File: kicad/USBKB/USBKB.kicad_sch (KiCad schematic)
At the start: 70 parts, among them K0 KAILH_CPG151101S11, K1 KAILH_CPG151101S11, K2 KAILH_CPG151101S11, K3 KAILH_CPG151101S11, K4 KAILH_CPG151101S11, K5 KAILH_CPG151101S11, K6 KAILH_CPG151101S11, K7 KAILH_CPG151101S11, K8 KAILH_CPG151101S11, K9 KAILH_CPG151101S11, U1 ATMEGA32U4-MU, U2 ICSP, U70 UJ31-CH-G2-SMT-TR, Y1 Crystal_GND23

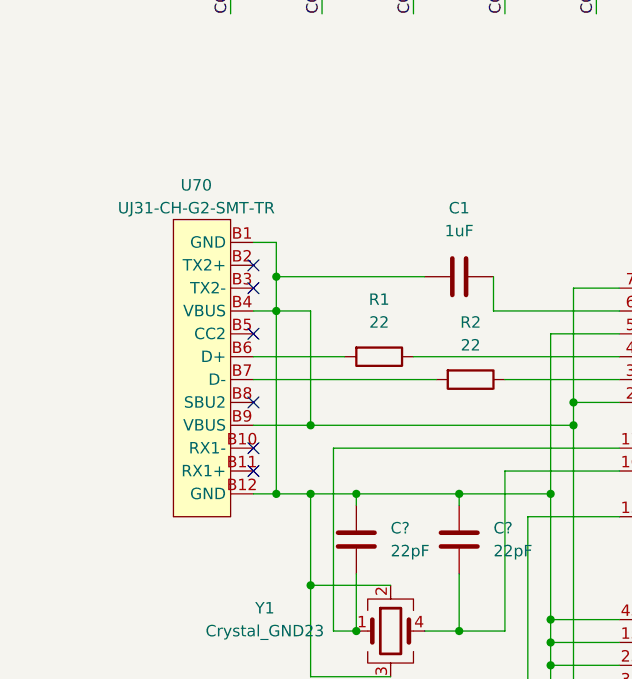
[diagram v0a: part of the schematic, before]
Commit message: Fixed USB-C connector in schematic
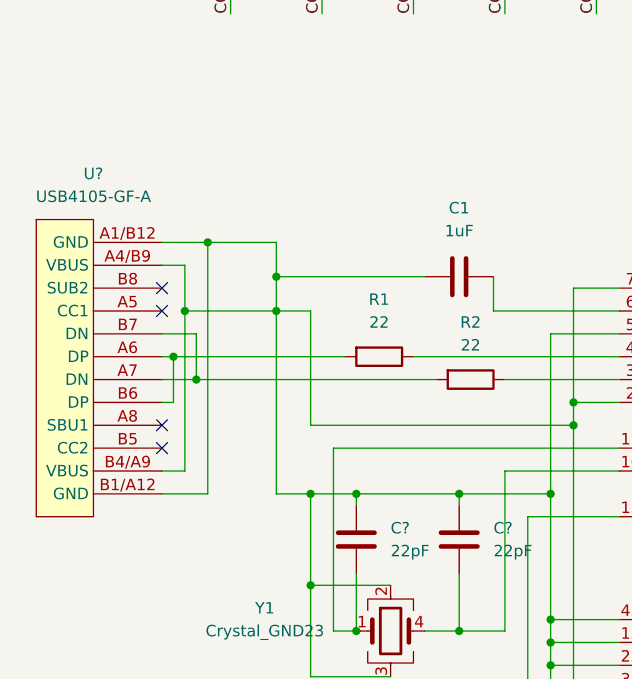
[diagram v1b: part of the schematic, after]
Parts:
- U?: renamed from U70; value UJ31-CH-G2-SMT-TR -> USB4105-GF-A; symbol USBKB:UJ31-CH-G2-SMT-TR -> USBKB:USB4105-GF-A
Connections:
- net at C1.1, C?.1, C?.1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: now also U?.A1/B12 (GND), U?.A4/B9 (VBUS), U?.B1/A12 (GND), U?.B4/A9 (VBUS); no longer U?.B1 (GND), U?.B12 (GND), U?.B4 (VBUS), U?.B9 (VBUS)
- net at R2.2, U?.B7 (DN): now also U?.A7 (DN)
- net at R1.2, U?.B6 (DP): now also U?.A6 (DP)
- no-connect marks 13 -> 11
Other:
- moved on the sheet: U?
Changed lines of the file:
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@@
   (junction (at 76.2 41.91) (diameter 0) (color 0 0 0 0)
   )
+  (junction (at 31.75 109.22) (diameter 0) (color 0 0 0 0)
+  )
   (junction (at 119.38 52.07) (diameter 0) (color 0 0 0 0)
   )
@@
   (junction (at 78.74 60.96) (diameter 0) (color 0 0 0 0)
   )
+  (junction (at 33.02 93.98) (diameter 0) (color 0 0 0 0)
+  )
   (junction (at 55.88 33.02) (diameter 0) (color 0 0 0 0)
   )
@@
   (junction (at 137.16 41.91) (diameter 0) (color 0 0 0 0)
   )
+  (junction (at 30.48 101.6) (diameter 0) (color 0 0 0 0)
+  )
   (junction (at 129.54 25.4) (diameter 0) (color 0 0 0 0)
   )
@@
   (junction (at 27.94 43.18) (diameter 0) (color 0 0 0 0)
   )
-  (junction (at 44.45 114.3) (diameter 0) (color 0 0 0 0)
-  )
   (junction (at 116.84 33.02) (diameter 0) (color 0 0 0 0)
   )
@@
   (junction (at 44.45 132.08) (diameter 0) (color 0 0 0 0)
   )
+  (junction (at 29.21 106.68) (diameter 0) (color 0 0 0 0)
+  )
   (junction (at 38.1 60.96) (diameter 0) (color 0 0 0 0)
   )
@@
   (junction (at 68.58 25.4) (diameter 0) (color 0 0 0 0)
   )
-  (junction (at 40.64 121.92) (diameter 0) (color 0 0 0 0)
-  )
   (junction (at 58.42 34.29) (diameter 0) (color 0 0 0 0)
   )
@@
   (junction (at 66.04 33.02) (diameter 0) (color 0 0 0 0)
   )
-  (no_connect (at 38.1 104.14))
-  (no_connect (at 38.1 99.06))
-  (no_connect (at 38.1 116.84))
-  (no_connect (at 38.1 119.38))
-  (no_connect (at 38.1 96.52))
-  (no_connect (at 38.1 111.76))
+  (no_connect (at 27.94 114.3))
+  (no_connect (at 27.94 116.84))
+  (no_connect (at 27.94 101.6))
+  (no_connect (at 27.94 99.06))
   (no_connect (at 121.92 95.25))
   (no_connect (at 121.92 146.05))
@@
     (stroke (width 0) (type default) (color 0 0 0 0))
   )
-  (wire (pts (xy 38.1 121.92) (xy 40.64 121.92))
-    (stroke (width 0) (type default) (color 0 0 0 0))
-  )
   (wire (pts (xy 149.86 24.13) (xy 149.86 25.4))
     (stroke (width 0) (type default) (color 0 0 0 0))
   )
+  (wire (pts (xy 33.02 121.92) (xy 33.02 93.98))
+    (stroke (width 0) (type default) (color 0 0 0 0))
+  )
   (wire (pts (xy 40.64 101.6) (xy 40.64 121.92))
     (stroke (width 0) (type default) (color 0 0 0 0))
@@
     (stroke (width 0) (type default) (color 0 0 0 0))
   )
+  (wire (pts (xy 29.21 111.76) (xy 29.21 106.68))
+    (stroke (width 0) (type default) (color 0 0 0 0))
+  )
   (wire (pts (xy 68.58 34.29) (xy 68.58 33.02))
     (stroke (width 0) (type default) (color 0 0 0 0))
@@
     (stroke (width 0) (type default) (color 0 0 0 0))
   )
-  (wire (pts (xy 38.1 106.68) (xy 48.26 106.68))
+  (wire (pts (xy 29.21 106.68) (xy 48.26 106.68))
     (stroke (width 0) (type default) (color 0 0 0 0))
   )
@@
     (stroke (width 0) (type default) (color 0 0 0 0))
   )
+  (wire (pts (xy 31.75 104.14) (xy 27.94 104.14))
+    (stroke (width 0) (type default) (color 0 0 0 0))
+  )
   (wire (pts (xy 48.26 52.07) (xy 58.42 52.07))
     (stroke (width 0) (type default) (color 0 0 0 0))
@@
     (stroke (width 0) (type default) (color 0 0 0 0))
   )
-  (wire (pts (xy 38.1 101.6) (xy 40.64 101.6))
+  (wire (pts (xy 30.48 101.6) (xy 40.64 101.6))
     (stroke (width 0) (type default) (color 0 0 0 0))
   )
@@
     (stroke (width 0) (type default) (color 0 0 0 0))
   )
+  (wire (pts (xy 27.94 109.22) (xy 31.75 109.22))
+    (stroke (width 0) (type default) (color 0 0 0 0))
+  )
   (wire (pts (xy 121.92 161.29) (xy 128.27 161.29))
     (stroke (width 0) (type default) (color 0 0 0 0))
@@
     (stroke (width 0) (type default) (color 0 0 0 0))
   )
-  (wire (pts (xy 38.1 114.3) (xy 44.45 114.3))
-    (stroke (width 0) (type default) (color 0 0 0 0))
-  )
   (wire (pts (xy 27.94 34.29) (xy 38.1 34.29))
     (stroke (width 0) (type default) (color 0 0 0 0))
@@
     (stroke (width 0) (type default) (color 0 0 0 0))
   )
+  (wire (pts (xy 27.94 96.52) (xy 30.48 96.52))
+    (stroke (width 0) (type default) (color 0 0 0 0))
+  )
   (wire (pts (xy 109.22 52.07) (xy 109.22 50.8))
     (stroke (width 0) (type default) (color 0 0 0 0))
@@
     (stroke (width 0) (type default) (color 0 0 0 0))
   )
+  (wire (pts (xy 31.75 109.22) (xy 31.75 104.14))
+    (stroke (width 0) (type default) (color 0 0 0 0))
+  )
   (wire (pts (xy 121.92 118.11) (xy 132.08 118.11))
     (stroke (width 0) (type default) (color 0 0 0 0))
@@
     (stroke (width 0) (type default) (color 0 0 0 0))
   )
-  (wire (pts (xy 40.64 93.98) (xy 38.1 93.98))
+  (wire (pts (xy 33.02 93.98) (xy 27.94 93.98))
+    (stroke (width 0) (type default) (color 0 0 0 0))
+  )
+  (wire (pts (xy 33.02 93.98) (xy 40.64 93.98))
     (stroke (width 0) (type default) (color 0 0 0 0))
   )
@@
     (stroke (width 0) (type default) (color 0 0 0 0))
   )
-  (wire (pts (xy 38.1 109.22) (xy 58.42 109.22))
+  (wire (pts (xy 31.75 109.22) (xy 58.42 109.22))
     (stroke (width 0) (type default) (color 0 0 0 0))
   )
@@
     (stroke (width 0) (type default) (color 0 0 0 0))
   )
+  (wire (pts (xy 30.48 119.38) (xy 27.94 119.38))
+    (stroke (width 0) (type default) (color 0 0 0 0))
+  )
   (wire (pts (xy 48.26 34.29) (xy 48.26 33.02))
     (stroke (width 0) (type default) (color 0 0 0 0))
@@
     (stroke (width 0) (type default) (color 0 0 0 0))
   )
+  (wire (pts (xy 27.94 121.92) (xy 33.02 121.92))
+    (stroke (width 0) (type default) (color 0 0 0 0))
+  )
   (wire (pts (xy 121.92 115.57) (xy 134.62 115.57))
     (stroke (width 0) (type default) (color 0 0 0 0))
@@
     (stroke (width 0) (type default) (color 0 0 0 0))
   )
+  (wire (pts (xy 30.48 96.52) (xy 30.48 101.6))
+    (stroke (width 0) (type default) (color 0 0 0 0))
+  )
   (wire (pts (xy 78.74 143.51) (xy 71.12 143.51))
     (stroke (width 0) (type default) (color 0 0 0 0))
   )
+  (wire (pts (xy 29.21 106.68) (xy 27.94 106.68))
+    (stroke (width 0) (type default) (color 0 0 0 0))
+  )
   (wire (pts (xy 129.54 43.18) (xy 139.7 43.18))
     (stroke (width 0) (type default) (color 0 0 0 0))
@@
     (stroke (width 0) (type default) (color 0 0 0 0))
   )
+  (wire (pts (xy 27.94 111.76) (xy 29.21 111.76))
+    (stroke (width 0) (type default) (color 0 0 0 0))
+  )
   (wire (pts (xy 129.54 60.96) (xy 139.7 60.96))
     (stroke (width 0) (type default) (color 0 0 0 0))
@@
   )
   (wire (pts (xy 55.88 106.68) (xy 78.74 106.68))
+    (stroke (width 0) (type default) (color 0 0 0 0))
+  )
+  (wire (pts (xy 30.48 101.6) (xy 30.48 119.38))
     (stroke (width 0) (type default) (color 0 0 0 0))
   )
@@
     (pin "2")
   )
-  (symbol (lib_id "USBKB:UJ31-CH-G2-SMT-TR") (at 35.56 107.95 0) (unit 1)
-    (in_bom yes) (on_board yes) (fields_autoplaced)
-    (property "Reference" "U70" (id 0) (at 31.75 87.63 0))
-    (property "Value" "UJ31-CH-G2-SMT-TR" (id 1) (at 31.75 90.17 0))
-    (property "Footprint" "USBKB:USB4105-GF-A" (id 2) (at 35.56 88.9 0)
-      (effects (font (size 1.27 1.27)) hide)
-    )
-    (property "Datasheet" "" (id 3) (at 35.56 88.9 0)
-      (effects (font (size 1.27 1.27)) hide)
-    )
-    (pin "B1")
-    (pin "B10")
-    (pin "B11")
-    (pin "B12")
-    (pin "B2")
-    (pin "B3")
-    (pin "B4")
+  (symbol (lib_id "USBKB:USB4105-GF-A") (at 20.32 99.06 0) (unit 1)
+    (in_bom yes) (on_board yes)
+    (property "Reference" "U?" (id 0) (at 20.32 86.36 0))
+    (property "Value" "USB4105-GF-A" (id 1) (at 20.32 88.9 0))
+    (property "Footprint" "USBKB:USB4105-GF-A" (id 2) (at 20.32 86.36 0)
+      (effects (font (size 1.27 1.27)) hide)
+    )
+    (property "Datasheet" "" (id 3) (at 20.32 86.36 0)
+      (effects (font (size 1.27 1.27)) hide)
+    )
+    (pin "A1/B12")
+    (pin "A4/B9")
+    (pin "A5")
+    (pin "A6")
+    (pin "A7")
+    (pin "A8")
+    (pin "B1/A12")
+    (pin "B4/A9")
     (pin "B5")
     (pin "B6")
     (pin "B7")
     (pin "B8")
-    (pin "B9")
   )
   (symbol (lib_id "USBKB:KAILH_CPG151101S11") (at 92.71 33.02 0) (unit 1)
@@
     )
     (path "/f359e712-bc14-4294-ae7c-f8c3b49e712a"
-      (reference "U70") (unit 1) (value "UJ31-CH-G2-SMT-TR") (footprint "USBKB:USB4105-GF-A")
+      (reference "U?") (unit 1) (value "USB4105-GF-A") (footprint "USBKB:USB4105-GF-A")
     )
     (path "/f8aa7b9d-0275-447c-a33e-2d8cb13a8083"

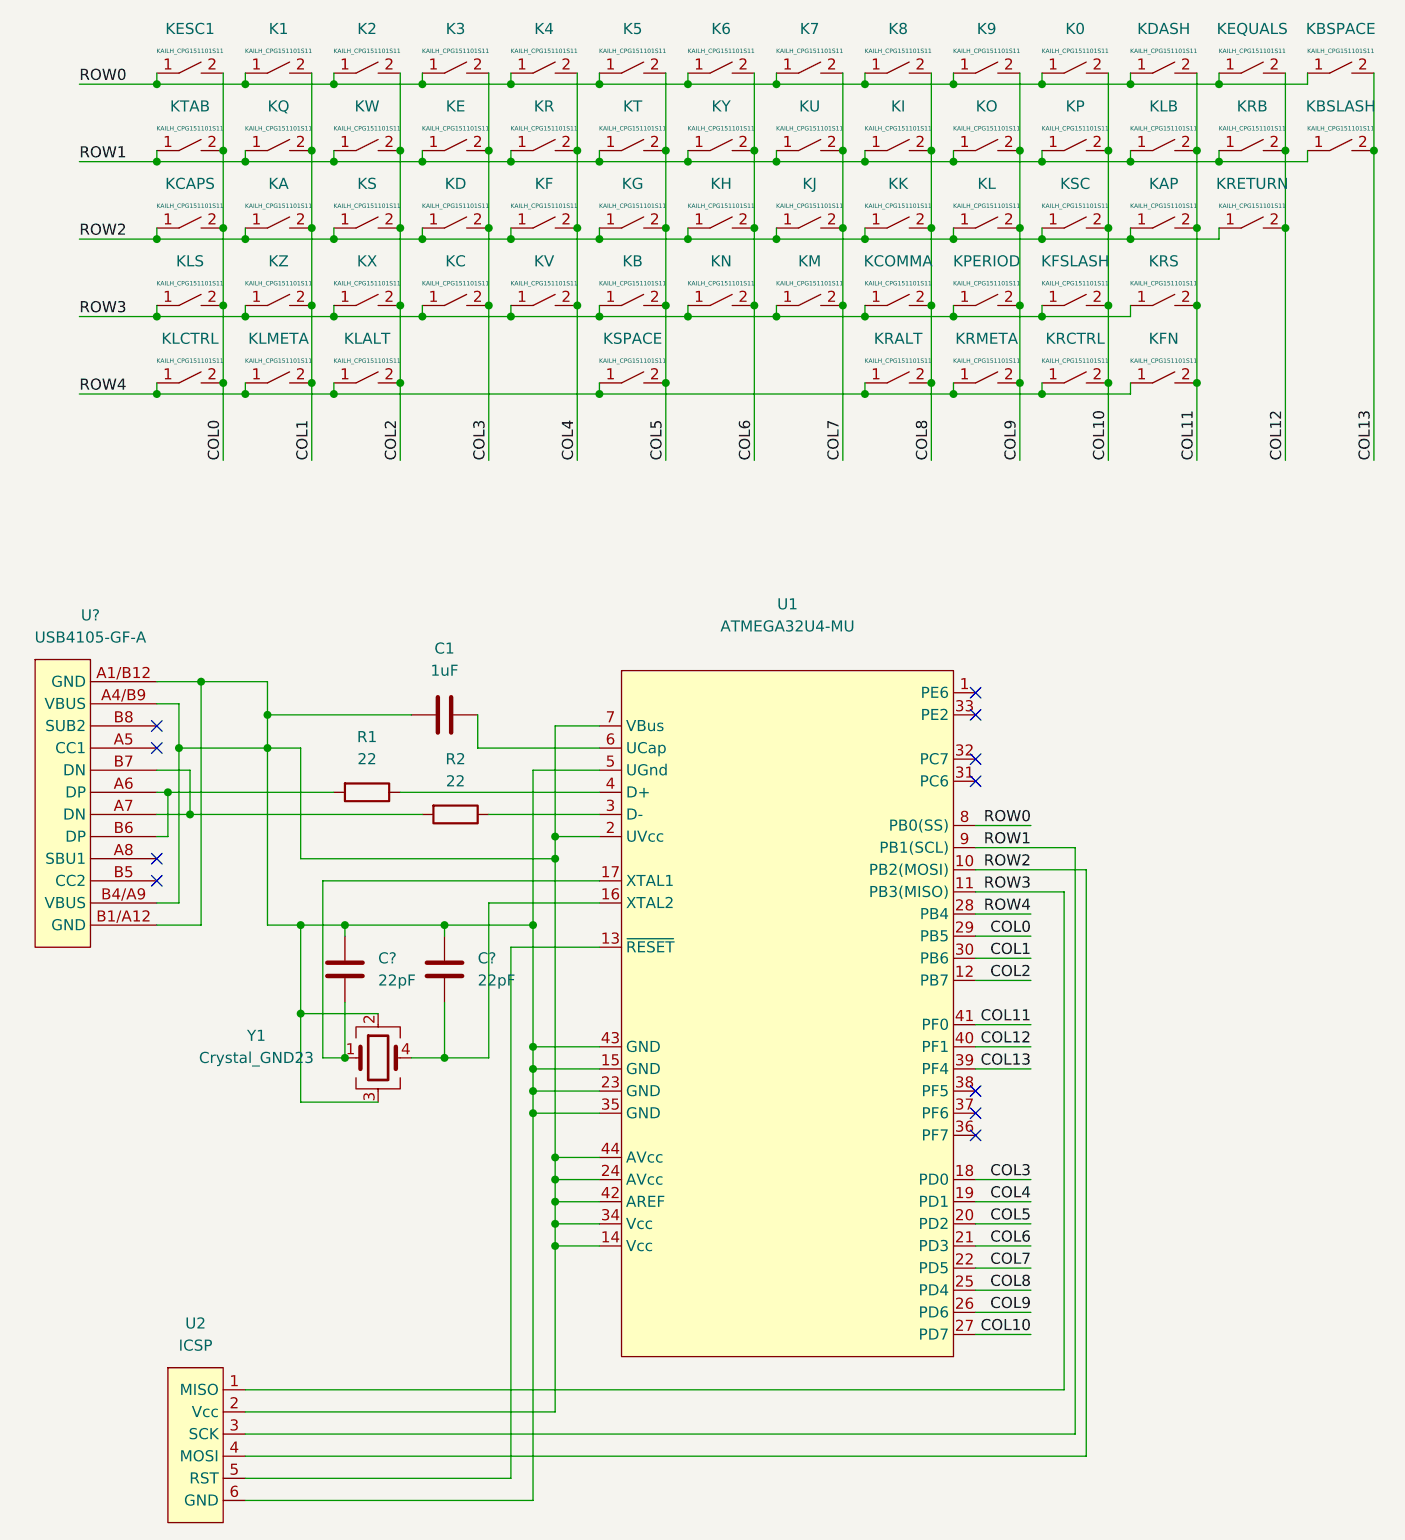
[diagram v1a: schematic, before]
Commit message: Began PCB alignment
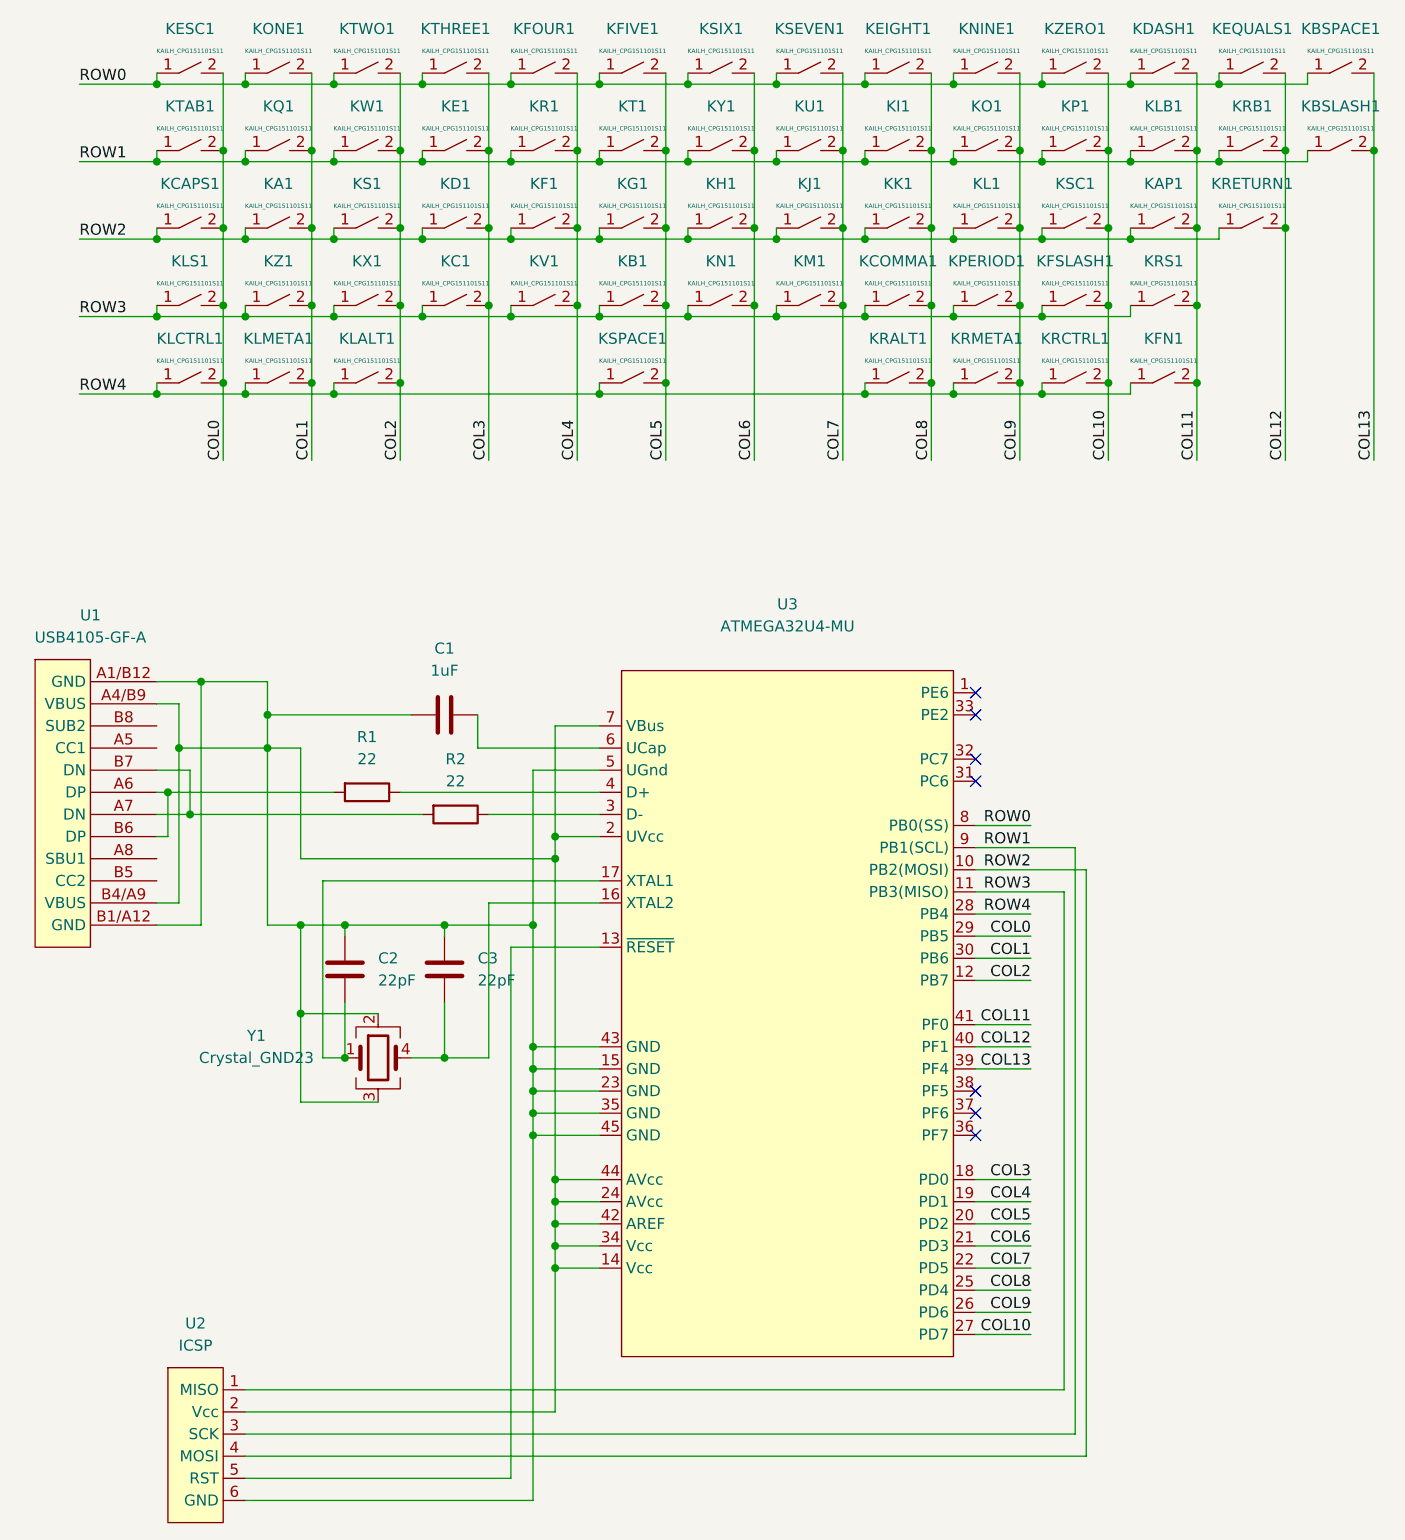
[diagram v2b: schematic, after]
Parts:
- gave numbers to parts that had none: 3
- renumbered KA to KA1, KAP to KAP1, KB to KB1, KBSLASH to KBSLASH1, KBSPACE to KBSPACE1, KC to KC1, KCAPS to KCAPS1, KCOMMA to KCOMMA1, KD to KD1, KDASH to KDASH1, KE to KE1, K8 to KEIGHT1, KEQUALS to KEQUALS1, KF to KF1, K5 to KFIVE1, KFN to KFN1, K4 to KFOUR1, KFSLASH to KFSLASH1, KG to KG1, KH to KH1, KI to KI1, KJ to KJ1, KK to KK1, KL to KL1, KLALT to KLALT1, KLB to KLB1, KLCTRL to KLCTRL1, KLMETA to KLMETA1, KLS to KLS1, KM to KM1, KN to KN1, K9 to KNINE1, KO to KO1, K1 to KONE1, KP to KP1, KPERIOD to KPERIOD1, KQ to KQ1, KR to KR1, KRALT to KRALT1, KRB to KRB1, KRCTRL to KRCTRL1, KRETURN to KRETURN1, KRMETA to KRMETA1, KRS to KRS1, KS to KS1, KSC to KSC1, K7 to KSEVEN1, K6 to KSIX1, KSPACE to KSPACE1, KT to KT1, KTAB to KTAB1, K3 to KTHREE1, K2 to KTWO1, KU to KU1, KV to KV1, KW to KW1, KX to KX1, KY to KY1, KZ to KZ1, K0 to KZERO1, U1 to U3
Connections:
- net at C1.1, C2.1, C3.1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: now also U3.45 (GND)
- no-connect marks 11 -> 7
